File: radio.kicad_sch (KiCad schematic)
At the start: 4 parts, among them J16 Conn_Coaxial, U11 E22-400M30S

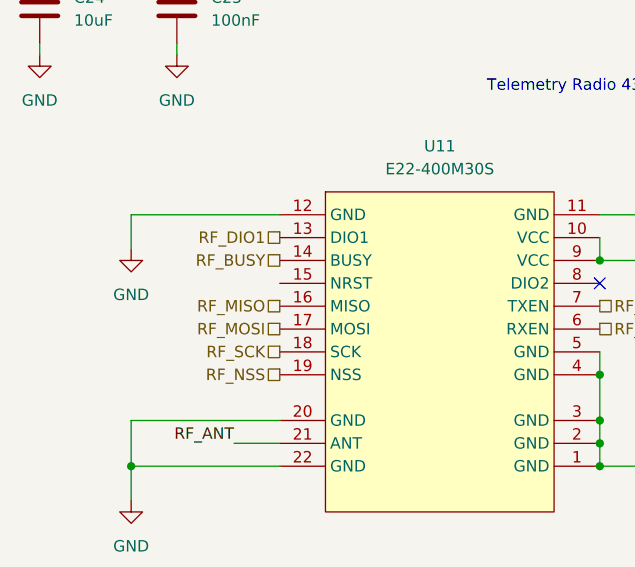
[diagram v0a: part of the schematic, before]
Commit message: Add more footprints!
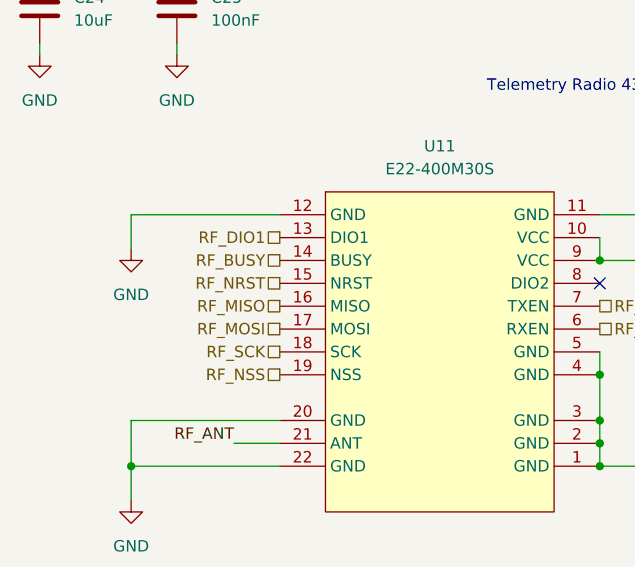
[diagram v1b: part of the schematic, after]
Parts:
- J16: footprint Connector_Coaxial:SMA_Amphenol_132289_EdgeMount -> Connector_Coaxial:SMA_Amphenol_901-144_Vertical
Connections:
- net RF_NRST: now reaches U11.15 (NRST)
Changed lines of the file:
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@@
+		)
+	)
+	(hierarchical_label "RF_NRST"
+		(shape passive)
+		(at 120.65 86.36 180)
+		(effects
+			(font
+				(size 1.27 1.27)
+			)
+			(justify right)
 		)
 	)
@@
 			)
 		)
-		(property "Footprint" "Connector_Coaxial:SMA_Amphenol_132289_EdgeMount"
+		(property "Footprint" "Connector_Coaxial:SMA_Amphenol_901-144_Vertical"
 			(at 162.56 127 0)
 			(effects

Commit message: Continue work
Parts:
- added C18: 1uF, Capacitor_SMD:C_0402_1005Metric_Pad0.74x0.62mm_HandSolder, symbol Device:C
- added C19: 100nF, Capacitor_SMD:C_0402_1005Metric_Pad0.74x0.62mm_HandSolder, symbol Device:C
- C24, C25: footprint Capacitor_SMD:C_0603_1608Metric -> Capacitor_SMD:C_0402_1005Metric_Pad0.74x0.62mm_HandSolder
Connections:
- net +5V: now also C18.1, C19.1
- net GND: now also C18.2, C19.2
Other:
- moved on the sheet: C24, C25

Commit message: Start PCB layout
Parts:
- U11: footprint SWIFTLIBS:WIRELM-SMD_E22-400M30S -> lcsc:WIRELM-SMD_E22-400M30S
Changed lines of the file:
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@@
 			)
 		)
-		(property "Footprint" "SWIFTLIBS:WIRELM-SMD_E22-400M30S"
+		(property "Footprint" "lcsc:WIRELM-SMD_E22-400M30S"
 			(at 138.43 114.3 0)
 			(effects
